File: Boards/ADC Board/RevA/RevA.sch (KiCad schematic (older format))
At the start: 0 parts

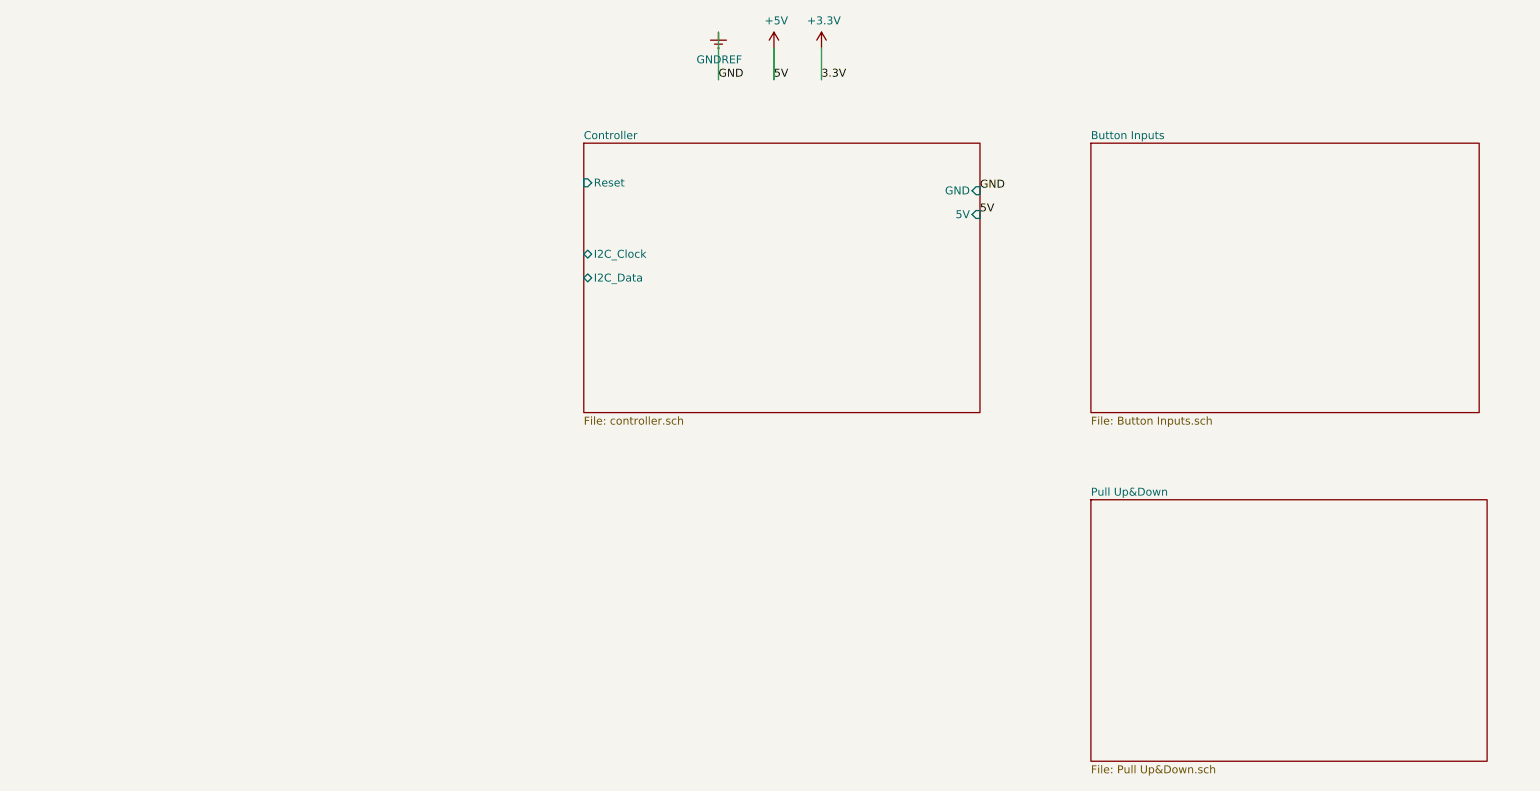
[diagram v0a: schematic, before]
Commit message: Copied controller board from micro board to ADC board. Created pull up/down sheets and populated them.
Also copied over main set of header pins into ADC sheet.
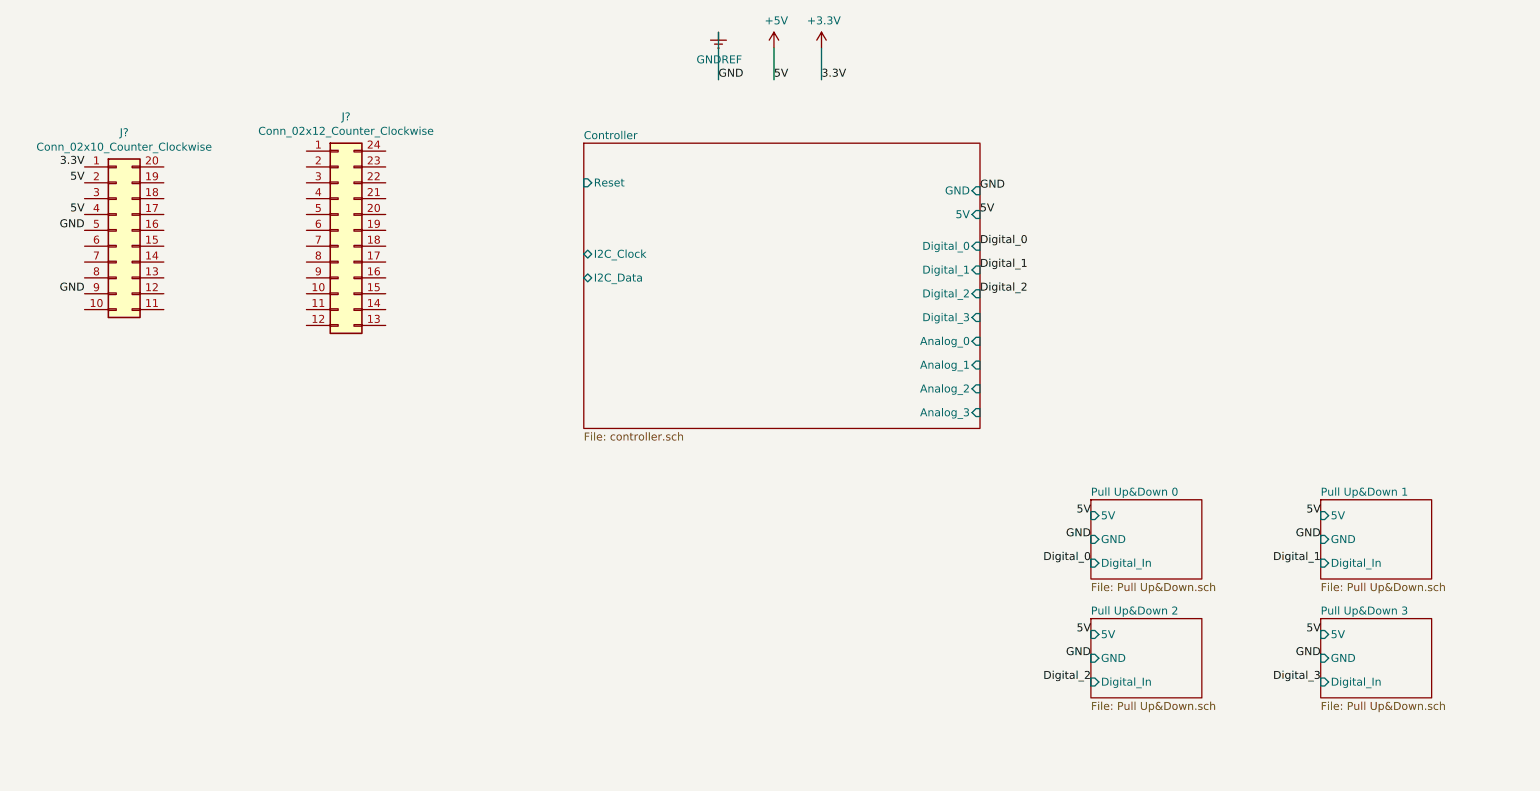
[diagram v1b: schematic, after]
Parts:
- added J?: Conn_02x10_Counter_Clockwise, symbol Connector_Generic:Conn_02x10_Counter_Clockwise
- added J?: Conn_02x12_Counter_Clockwise, symbol Connector_Generic:Conn_02x12_Counter_Clockwise
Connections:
- net +3V3: now also J?.1 (Pin_1)
- net +5V: now also J?.2 (Pin_2), J?.4 (Pin_4)
- net GNDREF: now also J?.5 (Pin_5), J?.9 (Pin_9)
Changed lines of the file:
@@
 $Descr A4 11693 8268
 encoding utf-8
-Sheet 1 4
+Sheet 1 6
 Title ""
 Date ""
@@
 Comment4 ""
 $EndDescr
-$Sheet
-S 4550 1300 2500 1700
-U 6158C434
-F0 "Controller" 50
-F1 "controller.sch" 50
-F2 "GND" I R 7050 1600 50
-F3 "5V" I R 7050 1750 50
-F4 "Reset" I L 4550 1550 50
-F5 "I2C_Clock" B L 4550 2000 50
-F6 "I2C_Data" B L 4550 2150 50
-$EndSheet
 Text Label 7050 1600 0    50   ~ 0
 GND
@@
 	6050 700  6050 900
 $Sheet
-S 7750 3550 2500 1650
+S 7750 3550 700  500
 U 61593BCA
-F0 "Pull Up&Down" 50
+F0 "Pull Up&Down 0" 50
 F1 "Pull Up&Down.sch" 50
+F2 "5V" I L 7750 3650 50
+F3 "GND" I L 7750 3800 50
+F4 "Digital_In" I L 7750 3950 50
+$EndSheet
+$Comp
+L Connector_Generic:Conn_02x10_Counter_Clockwise J?
+U 1 1 615E5E26
+P 1600 1850
+F 0 "J?" H 1650 2467 50  0000 C CNN
+F 1 "Conn_02x10_Counter_Clockwise" H 1650 2376 50  0000 C CNN
+F 2 "" H 1600 1850 50  0001 C CNN
+F 3 "~" H 1600 1850 50  0001 C CNN
+	1    1600 1850
+	1    0    0    -1
+$EndComp
+$Comp
+L Connector_Generic:Conn_02x12_Counter_Clockwise J?
+U 1 1 615E7214
+P 3000 1850
+F 0 "J?" H 3050 2567 50  0000 C CNN
+F 1 "Conn_02x12_Counter_Clockwise" H 3050 2476 50  0000 C CNN
+F 2 "" H 3000 1850 50  0001 C CNN
+F 3 "~" H 3000 1850 50  0001 C CNN
+	1    3000 1850
+	1    0    0    -1
+$EndComp
+Text Label 1400 1450 2    50   ~ 0
+3.3V
+Text Label 1400 1550 2    50   ~ 0
+5V
+Text Label 1400 1750 2    50   ~ 0
+5V
+Text Label 1400 1850 2    50   ~ 0
+GND
+Text Label 1400 2250 2    50   ~ 0
+GND
+$Sheet
+S 9200 3550 700  500
+U 616422A2
+F0 "Pull Up&Down 1" 50
+F1 "Pull Up&Down.sch" 50
+F2 "5V" I L 9200 3650 50
+F3 "GND" I L 9200 3800 50
+F4 "Digital_In" I L 9200 3950 50
 $EndSheet
 $Sheet
-S 7750 1300 2450 1700
-U 6159480C
-F0 "Button Inputs" 50
-F1 "Button Inputs.sch" 50
+S 7750 4300 700  500
+U 616423D2
+F0 "Pull Up&Down 2" 50
+F1 "Pull Up&Down.sch" 50
+F2 "5V" I L 7750 4400 50
+F3 "GND" I L 7750 4550 50
+F4 "Digital_In" I L 7750 4700 50
 $EndSheet
+$Sheet
+S 9200 4300 700  500
+U 616425FE
+F0 "Pull Up&Down 3" 50
+F1 "Pull Up&Down.sch" 50
+F2 "5V" I L 9200 4400 50
+F3 "GND" I L 9200 4550 50
+F4 "Digital_In" I L 9200 4700 50
+$EndSheet
+Text Label 7750 3650 2    50   ~ 0
+5V
+Text Label 7750 3800 2    50   ~ 0
+GND
+Text Label 7750 4400 2    50   ~ 0
+5V
+Text Label 7750 4550 2    50   ~ 0
+GND
+Text Label 9200 4400 2    50   ~ 0
+5V
+Text Label 9200 4550 2    50   ~ 0
+GND
+Text Label 9200 3650 2    50   ~ 0
+5V
+Text Label 9200 3800 2    50   ~ 0
+GND
+$Sheet
+S 4550 1300 2500 1800
+U 6158C434
+F0 "Controller" 50
+F1 "controller.sch" 50
+F2 "GND" I R 7050 1600 50
+F3 "5V" I R 7050 1750 50
+F4 "Reset" I L 4550 1550 50
+F5 "I2C_Clock" B L 4550 2000 50
+F6 "I2C_Data" B L 4550 2150 50
+F7 "Digital_2" I R 7050 2250 50
+F8 "Digital_1" I R 7050 2100 50
+F9 "Digital_3" I R 7050 2400 50
+F10 "Digital_0" I R 7050 1950 50
+F11 "Analog_0" I R 7050 2550 50
+F12 "Analog_1" I R 7050 2700 50
+F13 "Analog_2" I R 7050 2850 50
+F14 "Analog_3" I R 7050 3000 50
+$EndSheet
+Text Label 7750 3950 2    50   ~ 0
+Digital_0
+Text Label 9200 3950 2    50   ~ 0
+Digital_1
+Text Label 7750 4700 2    50   ~ 0
+Digital_2
+Text Label 9200 4700 2    50   ~ 0
+Digital_3
+Text Label 7050 1950 0    50   ~ 0
+Digital_0
+Text Label 7050 2100 0    50   ~ 0
+Digital_1
+Text Label 7050 2250 0    50   ~ 0
+Digital_2
 $EndSCHEMATC

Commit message: Created analog in sheets on ADC board, populated them, and connected them to controller.  Defined Interconnect pins. Placed mounting holes.
Converted some strain gauge connections to nets.
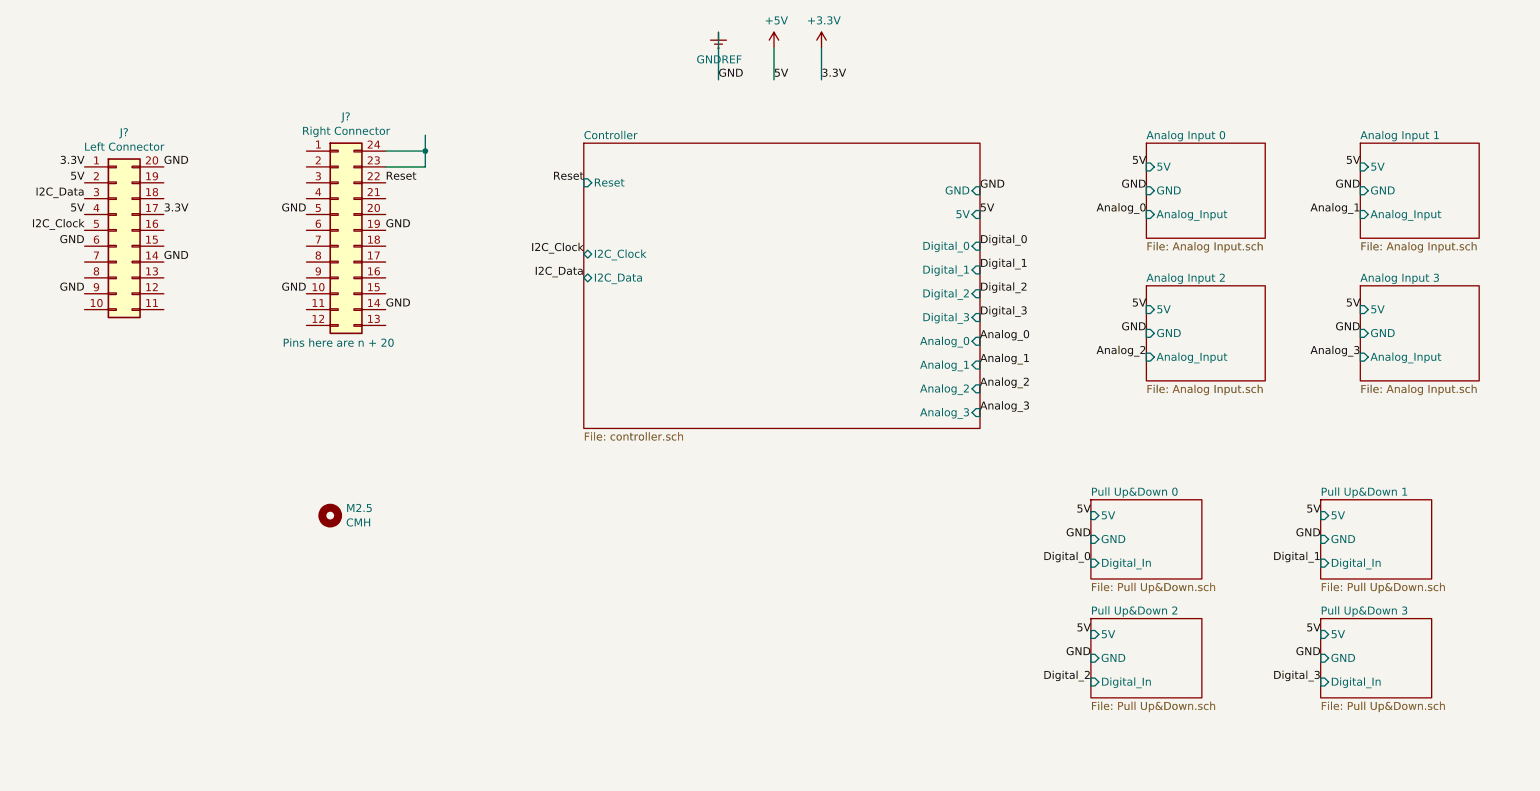
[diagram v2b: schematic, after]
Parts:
- added M2.5: CMH, symbol Mechanical:MountingHole
- J?: value Conn_02x10_Counter_Clockwise -> Left Connector
- J?: value Conn_02x12_Counter_Clockwise -> Right Connector
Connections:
- net labels added: Analog_0, Analog_1, Analog_2, Analog_3, I2C_Clock, I2C_Data, Reset
- wire segments 3 -> 7
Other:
- note added: "Pins here are n + 20"
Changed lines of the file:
@@
 $Descr A4 11693 8268
 encoding utf-8
-Sheet 1 6
+Sheet 1 10
 Title ""
 Date ""
@@
 P 1600 1850
 F 0 "J?" H 1650 2467 50  0000 C CNN
-F 1 "Conn_02x10_Counter_Clockwise" H 1650 2376 50  0000 C CNN
+F 1 "Left Connector" H 1650 2376 50  0000 C CNN
 F 2 "" H 1600 1850 50  0001 C CNN
 F 3 "~" H 1600 1850 50  0001 C CNN
@@
 P 3000 1850
 F 0 "J?" H 3050 2567 50  0000 C CNN
-F 1 "Conn_02x12_Counter_Clockwise" H 3050 2476 50  0000 C CNN
+F 1 "Right Connector" H 3050 2476 50  0000 C CNN
 F 2 "" H 3000 1850 50  0001 C CNN
 F 3 "~" H 3000 1850 50  0001 C CNN
@@
 Text Label 1400 1750 2    50   ~ 0
 5V
-Text Label 1400 1850 2    50   ~ 0
+Text Label 1400 1950 2    50   ~ 0
 GND
 Text Label 1400 2250 2    50   ~ 0
@@
 Text Label 7050 2250 0    50   ~ 0
 Digital_2
+Text Label 7050 2400 0    50   ~ 0
+Digital_3
+$Sheet
+S 8100 1300 750  600
+U 6164D83E
+F0 "Analog Input 0" 50
+F1 "Analog Input.sch" 50
+F2 "5V" I L 8100 1450 50
+F3 "GND" I L 8100 1600 50
+F4 "Analog_Input" I L 8100 1750 50
+$EndSheet
+Text Label 7050 2550 0    50   ~ 0
+Analog_0
+Text Label 8100 1750 2    50   ~ 0
+Analog_0
+Text Label 8100 1600 2    50   ~ 0
+GND
+Text Label 8100 1450 2    50   ~ 0
+5V
+$Sheet
+S 9450 1300 750  600
+U 616568DC
+F0 "Analog Input 1" 50
+F1 "Analog Input.sch" 50
+F2 "5V" I L 9450 1450 50
+F3 "GND" I L 9450 1600 50
+F4 "Analog_Input" I L 9450 1750 50
+$EndSheet
+Text Label 9450 1750 2    50   ~ 0
+Analog_1
+Text Label 9450 1600 2    50   ~ 0
+GND
+Text Label 9450 1450 2    50   ~ 0
+5V
+$Sheet
+S 8100 2200 750  600
+U 61657053
+F0 "Analog Input 2" 50
+F1 "Analog Input.sch" 50
+F2 "5V" I L 8100 2350 50
+F3 "GND" I L 8100 2500 50
+F4 "Analog_Input" I L 8100 2650 50
+$EndSheet
+Text Label 8100 2500 2    50   ~ 0
+GND
+Text Label 8100 2350 2    50   ~ 0
+5V
+$Sheet
+S 9450 2200 750  600
+U 616571E9
+F0 "Analog Input 3" 50
+F1 "Analog Input.sch" 50
+F2 "5V" I L 9450 2350 50
+F3 "GND" I L 9450 2500 50
+F4 "Analog_Input" I L 9450 2650 50
+$EndSheet
+Text Label 9450 2500 2    50   ~ 0
+GND
+Text Label 9450 2350 2    50   ~ 0
+5V
+Text Label 7050 2700 0    50   ~ 0
+Analog_1
+Text Label 8100 2650 2    50   ~ 0
+Analog_2
+Text Label 7050 2850 0    50   ~ 0
+Analog_2
+Text Label 9450 2650 2    50   ~ 0
+Analog_3
+Text Label 7050 3000 0    50   ~ 0
+Analog_3
+Text Label 1900 1450 0    50   ~ 0
+GND
+Text Label 1900 2050 0    50   ~ 0
+GND
+Text Label 1900 1750 0    50   ~ 0
+3.3V
+Text Label 2800 1750 2    50   ~ 0
+GND
+Text Label 2800 2250 2    50   ~ 0
+GND
+Text Label 3300 2350 0    50   ~ 0
+GND
+Text Label 3300 1850 0    50   ~ 0
+GND
+Wire Wire Line
+	3550 1350 3550 1250
+Wire Wire Line
+	3300 1350 3550 1350
+Wire Wire Line
+	3550 1350 3550 1450
+Wire Wire Line
+	3550 1450 3300 1450
+Connection ~ 3550 1350
+Text Notes 2650 2600 0    50   ~ 0
+Pins here are n + 20
+Text Label 4550 1550 2    50   ~ 0
+Reset
+Text Label 3300 1550 0    50   ~ 0
+Reset
+Text Label 4550 2150 2    50   ~ 0
+I2C_Data
+Text Label 4550 2000 2    50   ~ 0
+I2C_Clock
+Text Label 1400 1650 2    50   ~ 0
+I2C_Data
+Text Label 1400 1850 2    50   ~ 0
+I2C_Clock
+$Comp
+L Mechanical:MountingHole M2.5
+U 1 1 616626E5
+P 2950 3650
+F 0 "M2.5" H 3050 3696 50  0000 L CNN
+F 1 "CMH" H 3050 3605 50  0000 L CNN
+F 2 "" H 2950 3650 50  0001 C CNN
+F 3 "~" H 2950 3650 50  0001 C CNN
+	1    2950 3650
+	1    0    0    -1
+$EndComp
 $EndSCHEMATC

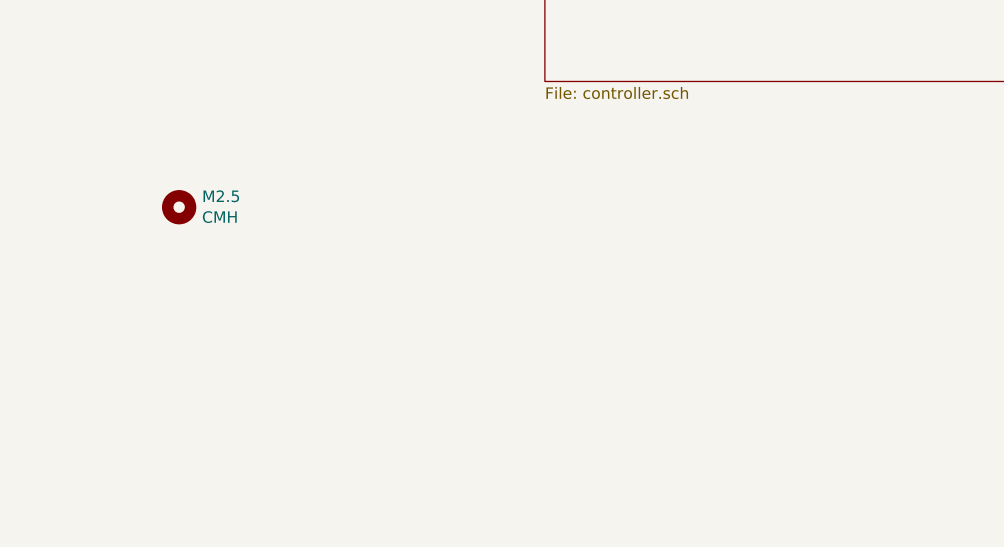
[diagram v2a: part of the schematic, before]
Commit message: Added regulator to ADC and micro boards. Added actual connectors for the strain gauge modules.
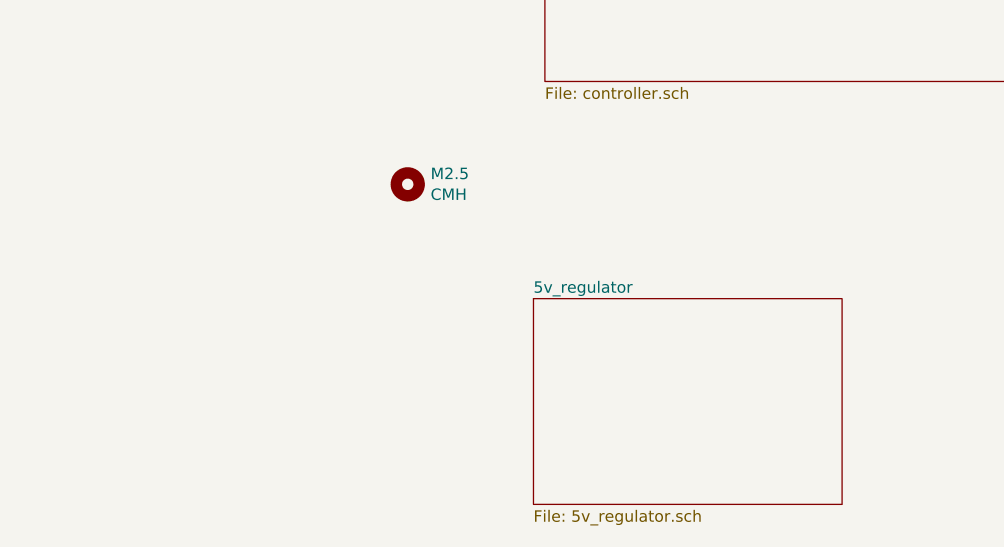
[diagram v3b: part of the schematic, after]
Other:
- moved on the sheet: M2.5
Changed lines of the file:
@@
 $Descr A4 11693 8268
 encoding utf-8
-Sheet 1 10
+Sheet 1 11
 Title ""
 Date ""
@@
 L Mechanical:MountingHole M2.5
 U 1 1 616626E5
-P 2950 3650
-F 0 "M2.5" H 3050 3696 50  0000 L CNN
-F 1 "CMH" H 3050 3605 50  0000 L CNN
-F 2 "" H 2950 3650 50  0001 C CNN
-F 3 "~" H 2950 3650 50  0001 C CNN
-	1    2950 3650
-	1    0    0    -1
-$EndComp
+P 3950 3550
+F 0 "M2.5" H 4050 3596 50  0000 L CNN
+F 1 "CMH" H 4050 3505 50  0000 L CNN
+F 2 "" H 3950 3550 50  0001 C CNN
+F 3 "~" H 3950 3550 50  0001 C CNN
+	1    3950 3550
+	1    0    0    -1
+$EndComp
+$Sheet
+S 4500 4050 1350 900
+U 61663709
+F0 "5v_regulator" 50
+F1 "5v_regulator.sch" 50
+$EndSheet
 $EndSCHEMATC
